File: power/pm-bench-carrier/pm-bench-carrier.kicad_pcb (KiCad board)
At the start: 2 copper layers, 130 x 55 mm, 45 parts, among them J1 VIN 40-60V, J2 VOUT 19V, Q1 2N7002, X1 PM-19V-200W, X2 Aux socket

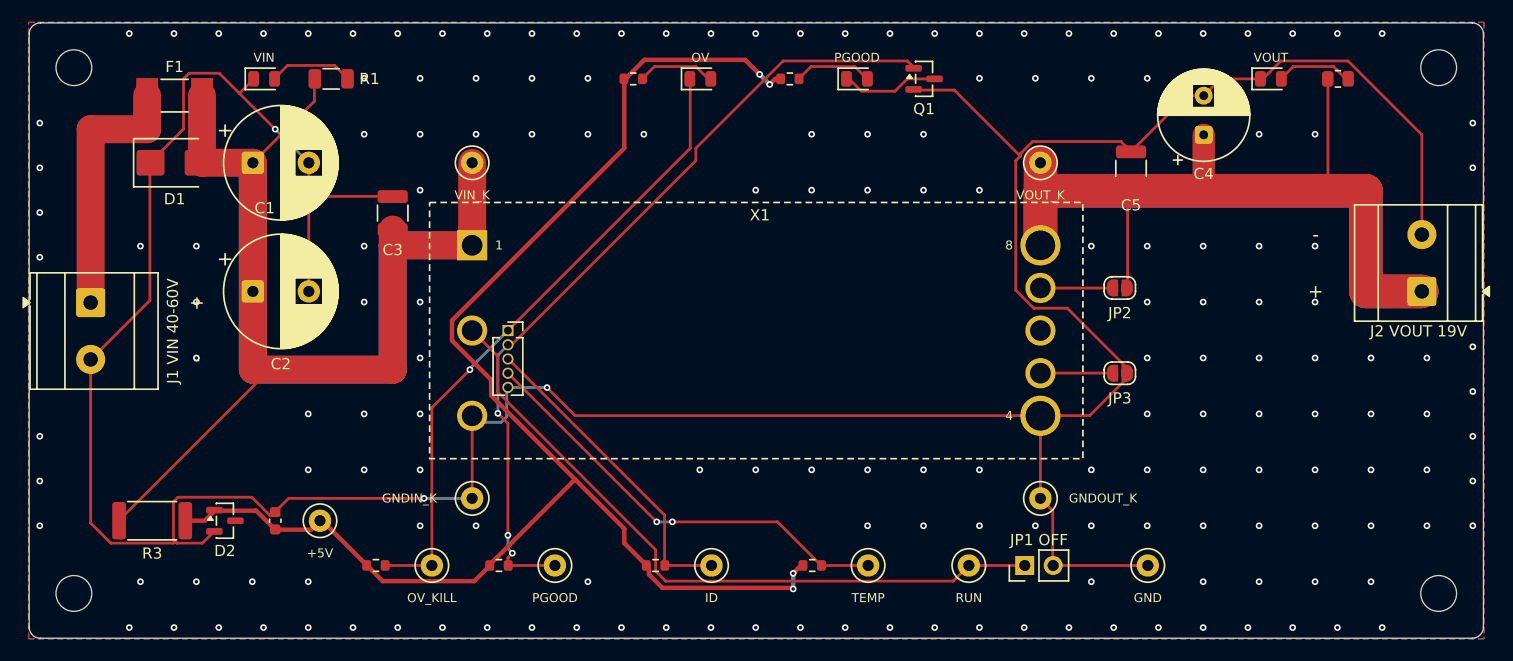
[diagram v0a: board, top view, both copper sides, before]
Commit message: pm-bench-carrier: pour GND before routing so KRT draws no GND tracks (zones kept via group power); DRC clean, 0 GND tracks
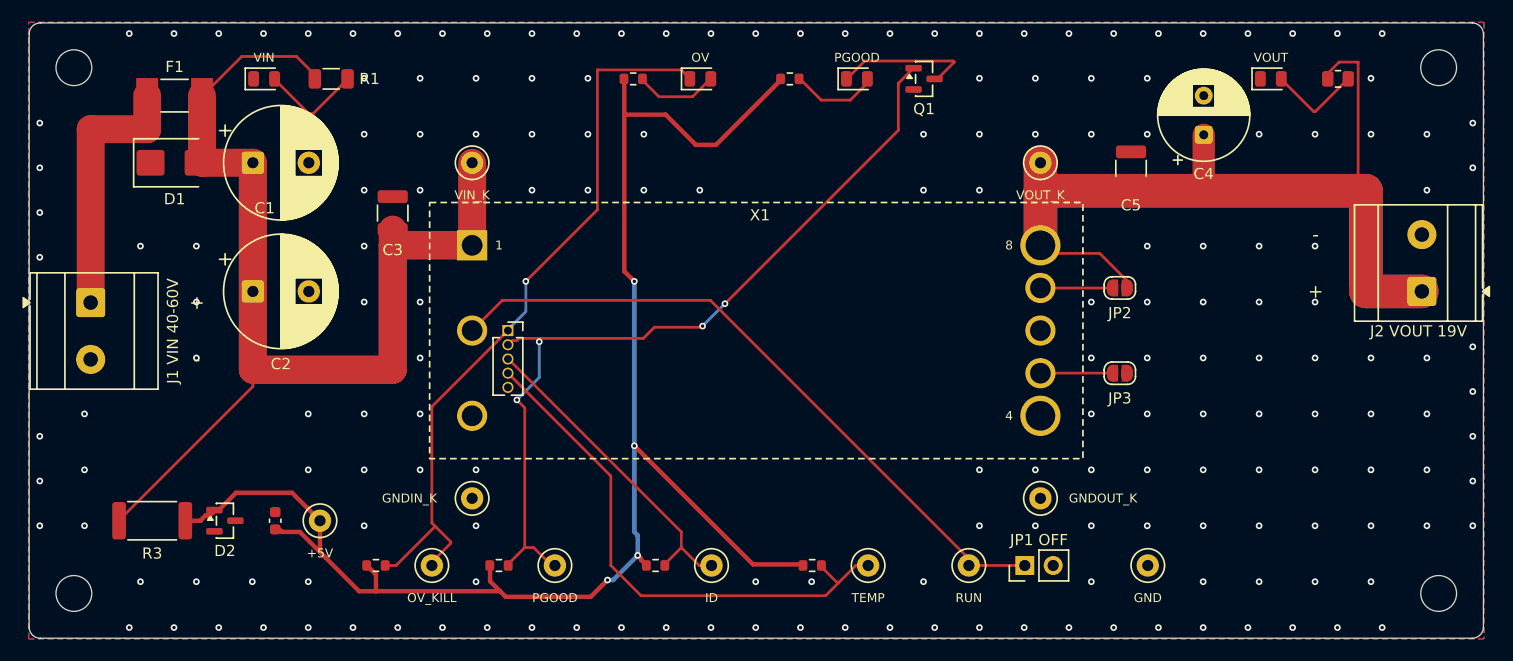
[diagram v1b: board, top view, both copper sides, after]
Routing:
- net GND: track 304.1 -> 0.00 mm, vias 172 -> 180
- net /TEMP: track 39.3 -> 48.4 mm, vias 2 -> 0
- net /OV_KILL: track 57.2 -> 66.0 mm
- net +5V: track 131.1 -> 139.1 mm
- net /VOUT: track 122.2 -> 128.4 mm
- net Net-(LED4-K): track 8.55 -> 12.4 mm
- net /RUN: track 62.2 -> 59.8 mm
- net /VIN: track 146.7 -> 148.4 mm
- net Net-(LED2-A): track 6.71 -> 8.40 mm
- net Net-(LED1-A): track 7.59 -> 9.17 mm
- net /PGOOD: track 72.4 -> 73.6 mm, vias 3 -> 4
- net Net-(LED3-A): track 6.81 -> 7.38 mm

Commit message: pm-bench-carrier: LCSC numbers on the SMD parts, fuse 10 A (0451010.MRL); jlcfab BOM/CPL filled
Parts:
- F1: value 8A 125V nano2 -> 10A 125V nano2
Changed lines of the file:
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@@
 			)
 		)
+		(property "LCSC" "C25803"
+			(at 0 0 0)
+			(layer "F.Fab")
+			(hide yes)
+			(effects
+				(font
+					(size 1.27 1.27)
+				)
+			)
+		)
 		(sheetname "pm-bench-carrier")
 		(sheetfile "pm-bench-carrier.kicad_sch")
@@
 			)
 		)
+		(property "LCSC" "C84256"
+			(at 0 0 0)
+			(layer "F.Fab")
+			(hide yes)
+			(effects
+				(font
+					(size 1.27 1.27)
+				)
+			)
+		)
 		(sheetname "pm-bench-carrier")
 		(sheetfile "pm-bench-carrier.kicad_sch")
@@
 			)
 		)
+		(property "LCSC" "C270956"
+			(at 0 0 0)
+			(layer "F.Fab")
+			(hide yes)
+			(effects
+				(font
+					(size 1.27 1.27)
+				)
+			)
+		)
 		(sheetname "pm-bench-carrier")
 		(sheetfile "pm-bench-carrier.kicad_sch")
@@
 			)
 		)
-		(property "Value" "8A 125V nano2"
+		(property "Value" "10A 125V nano2"
 			(at 0 2.7 0)
 			(unlocked yes)
@@
 			)
 		)
+		(property "LCSC" "C44479"
+			(at 0 0 0)
+			(layer "F.Fab")
+			(hide yes)
+			(effects
+				(font
+					(size 1.27 1.27)
+				)
+			)
+		)
 		(sheetname "pm-bench-carrier")
 		(sheetfile "pm-bench-carrier.kicad_sch")
@@
 			)
 		)
+		(property "LCSC" "C22978"
+			(at 0 0 0)
+			(layer "F.Fab")
+			(hide yes)
+			(effects
+				(font
+					(size 1.27 1.27)
+				)
+			)
+		)
 		(sheetname "pm-bench-carrier")
 		(sheetfile "pm-bench-carrier.kicad_sch")
@@
 			)
 		)
+		(property "LCSC" "C55151"
+			(at 0 0 0)
+			(layer "F.Fab")
+			(hide yes)
+			(effects
+				(font
+					(size 1.27 1.27)
+				)
+			)
+		)
 		(sheetname "pm-bench-carrier")
 		(sheetfile "pm-bench-carrier.kicad_sch")
@@
 			)
 		)
+		(property "LCSC" "C15849"
+			(at 0 0 0)
+			(layer "F.Fab")
+			(hide yes)
+			(effects
+				(font
+					(size 1.27 1.27)
+				)
+			)
+		)
 		(sheetname "pm-bench-carrier")
 		(sheetfile "pm-bench-carrier.kicad_sch")
@@
 			)
 		)
+		(property "LCSC" "C17943"
+			(at 0 0 0)
+			(layer "F.Fab")
+			(hide yes)
+			(effects
+				(font
+					(size 1.27 1.27)
+				)
+			)
+		)
 		(sheetname "pm-bench-carrier")
 		(sheetfile "pm-bench-carrier.kicad_sch")
@@
 			)
 		)
+		(property "LCSC" "C353345"
+			(at 0 0 0)
+			(layer "F.Fab")
+			(hide yes)
+			(effects
+				(font
+					(size 1.27 1.27)
+				)
+			)
+		)
 		(sheetname "pm-bench-carrier")
 		(sheetfile "pm-bench-carrier.kicad_sch")
@@
 			)
 		)
+		(property "LCSC" "C17414"
+			(at 0 0 0)
+			(layer "F.Fab")
+			(hide yes)
+			(effects
+				(font
+					(size 1.27 1.27)
+				)
+			)
+		)
 		(sheetname "pm-bench-carrier")
 		(sheetfile "pm-bench-carrier.kicad_sch")
@@
 			)
 		)
+		(property "LCSC" "C22978"
+			(at 0 0 0)
+			(layer "F.Fab")
+			(hide yes)
+			(effects
+				(font
+					(size 1.27 1.27)
+				)
+			)
+		)
 		(sheetname "pm-bench-carrier")
 		(sheetfile "pm-bench-carrier.kicad_sch")
@@
 			)
 		)
+		(property "LCSC" "C2297"
+			(at 0 0 0)
+			(layer "F.Fab")
+			(hide yes)
+			(effects
+				(font
+					(size 1.27 1.27)
+				)
+			)
+		)
 		(sheetname "pm-bench-carrier")
 		(sheetfile "pm-bench-carrier.kicad_sch")
@@
 			)
 		)
+		(property "LCSC" "C27131"
+			(at 0 0 0)
+			(layer "F.Fab")
+			(hide yes)
+			(effects
+				(font
+					(size 1.27 1.27)
+				)
+			)
+		)
 		(sheetname "pm-bench-carrier")
 		(sheetfile "pm-bench-carrier.kicad_sch")
@@
 			)
 		)
+		(property "LCSC" "C2297"
+			(at 0 0 0)
+			(layer "F.Fab")
+			(hide yes)
+			(effects
+				(font
+					(size 1.27 1.27)
+				)
+			)
+		)
 		(sheetname "pm-bench-carrier")
 		(sheetfile "pm-bench-carrier.kicad_sch")
@@
 			)
 		)
+		(property "LCSC" "C2297"
+			(at 0 0 0)
+			(layer "F.Fab")
+			(hide yes)
+			(effects
+				(font
+					(size 1.27 1.27)
+				)
+			)
+		)
 		(sheetname "pm-bench-carrier")
 		(sheetfile "pm-bench-carrier.kicad_sch")
@@
 			)
 		)
+		(property "LCSC" "C25804"
+			(at 0 0 0)
+			(layer "F.Fab")
+			(hide yes)
+			(effects
+				(font
+					(size 1.27 1.27)
+				)
+			)
+		)
 		(sheetname "pm-bench-carrier")
 		(sheetfile "pm-bench-carrier.kicad_sch")
@@
 			)
 		)
+		(property "LCSC" "C25803"
+			(at 0 0 0)
+			(layer "F.Fab")
+			(hide yes)
+			(effects
+				(font
+					(size 1.27 1.27)
+				)
+			)
+		)
 		(sheetname "pm-bench-carrier")
 		(sheetfile "pm-bench-carrier.kicad_sch")
@@
 			)
 		)
+		(property "LCSC" "C2918502"
+			(at 0 0 0)
+			(layer "F.Fab")
+			(hide yes)
+			(effects
+				(font
+					(size 1.27 1.27)
+				)
+			)
+		)
 		(sheetname "pm-bench-carrier")
 		(sheetfile "pm-bench-carrier.kicad_sch")
@@
 			)
 		)
+		(property "LCSC" "C8545"
+			(at 0 0 0)
+			(layer "F.Fab")
+			(hide yes)
+			(effects
+				(font
+					(size 1.27 1.27)
+				)
+			)
+		)
 		(sheetname "pm-bench-carrier")
 		(sheetfile "pm-bench-carrier.kicad_sch")
@@
 				)
 			)
+		)
+		(property "LCSC" "C25804"
+			(at 0 0 0)
+			(layer "F.Fab")
+			(hide yes)
+			(effects
+				(font
+					(size 1.27 1.27)
+				)
+			)

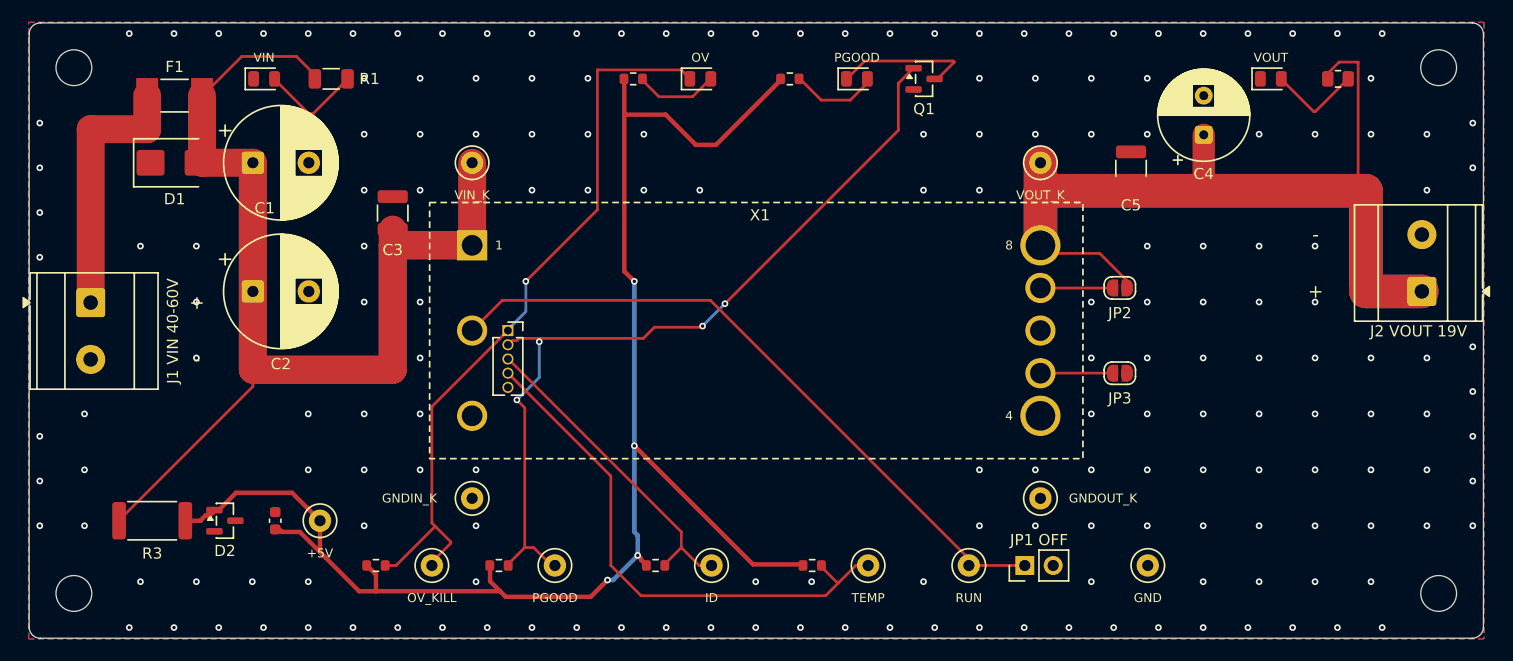
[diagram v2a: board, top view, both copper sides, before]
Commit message: pm-bench-carrier rev 0.2 board: screwed PM mount placed from pmmount.host_parts (SO1-SO4, PG1-PG6, MOD1 outline), trunks end on the standoffs, VOUT 4 mm for 13.2 A, Kelvin TPs at the screw x; rebuilt from the netlist and KRT-routed: DRC 0 errors, 0 unconnected, parity clean; docs and handoff updated
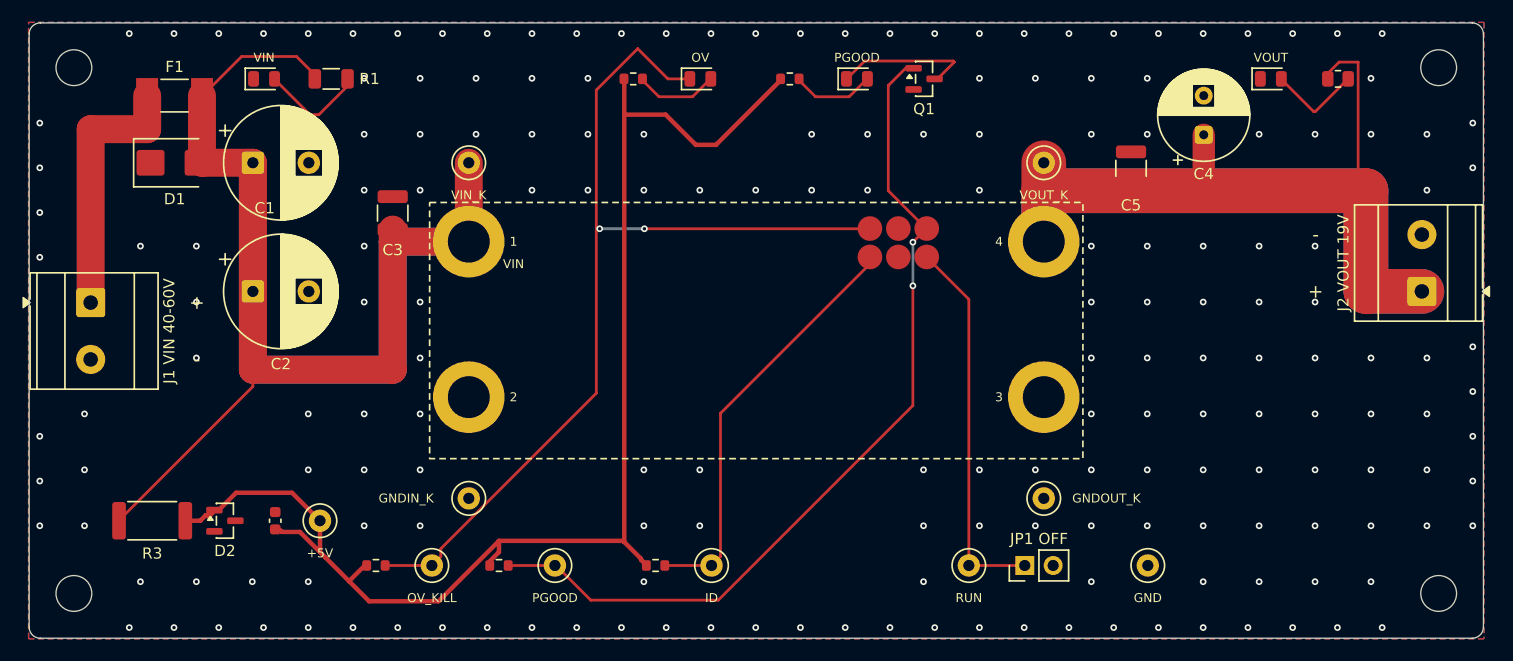
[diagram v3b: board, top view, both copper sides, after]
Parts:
- removed JP2: SENSE+, Jumper:SolderJumper-2_P1.3mm_Open_RoundedPad1.0x1.5mm
- removed JP3: SENSE-, Jumper:SolderJumper-2_P1.3mm_Open_RoundedPad1.0x1.5mm
- removed R9: 10k, Resistor_SMD:R_0603_1608Metric
- removed TP10: TEMP, TestPoint:TestPoint_Loop_D2.50mm_Drill1.0mm
- removed X1: PM-19V-200W, carrier:Brick_Eighth_DOSA_Socket
- removed X2: Aux socket, Connector_PinSocket_1.27mm:PinSocket_1x05_P1.27mm_Vertical
- added MOD1: PM_Module_Outline, carrier:PM_Module_Outline, F.Cu at (165.0, 127.5)
- added PG1: A1 OV_KILL, carrier:PM_Pogo_YZ130115073P, F.Cu at (175.2, 118.4)
- added PG2: A2 PGOOD, carrier:PM_Pogo_YZ130115073P, F.Cu at (180.2, 118.4)
- added PG3: A3 ID, carrier:PM_Pogo_YZ130115073P, F.Cu at (175.2, 120.9)
- added PG4: A4 RUN, carrier:PM_Pogo_YZ130115073P, F.Cu at (180.2, 120.9)
- added PG5: A5 GND, carrier:PM_Pogo_YZ130115073P, F.Cu at (177.7, 118.4)
- added PG6: A6 GND, carrier:PM_Pogo_YZ130115073P, F.Cu at (177.7, 120.9)
- added SO1: S1 VIN, carrier:PM_Standoff_M2x6_SMTSO, F.Cu at (139.3, 119.5)
- added SO2: S2 GND, carrier:PM_Standoff_M2x6_SMTSO, F.Cu at (139.3, 133.4)
- added SO3: S3 GND, carrier:PM_Standoff_M2x6_SMTSO, F.Cu at (190.7, 133.4)
- added SO4: S4 VOUT, carrier:PM_Standoff_M2x6_SMTSO, F.Cu at (190.7, 119.5)
- moved TP1 0.30 mm to (139.3, 112.5)
- moved TP2 0.30 mm to (139.3, 142.5)
- moved TP3 0.30 mm to (190.7, 112.5)
- moved TP4 0.30 mm to (190.7, 142.5)
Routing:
- net /TEMP: track 48.4 -> 0.00 mm
- net /RUN: track 59.8 -> 33.6 mm
- net /OV_KILL: track 66.0 -> 87.7 mm, vias 1 -> 2
- net +5V: track 139.1 -> 118.1 mm, vias 4 -> 0
- net /VOUT: track 128.4 -> 116.8 mm
- net /ID: track 28.8 -> 36.8 mm
- net Net-(JP3-A): track 6.00 -> 0.00 mm
- net Net-(JP2-A): track 6.00 -> 0.00 mm
- net /PGOOD: track 73.6 -> 77.0 mm, vias 4 -> 2
- net /VIN: track 148.4 -> 147.8 mm
- net GND: vias 180 -> 187
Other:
- board text removed: "TEMP"

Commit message: PM aux contacts: 2x3 1.27 mm SMT header (module J2, C41376035) into SMT socket (carrier J3, C41397112) replaces flat pads + pogos; standoffs M2 x 7 (C2916355), gap 7.0 mm. pmmount.py generates the new footprints; module J2 swapped in place, tools/route_aux.py moves PGOOD's via and adds a GND via between the columns (DRC as before, 0 unconnected, parity clean); carrier PG1-PG6 -> J3 and rebuilt by its flow (DRC 0 errors, 0 unconnected, parity clean); spec, ADR 0003 (6, 7), power-board.md and handoff updated; ID open = slot fault rule
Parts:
- removed PG1: A1 OV_KILL, carrier:PM_Pogo_YZ130115073P
- removed PG2: A2 PGOOD, carrier:PM_Pogo_YZ130115073P
- removed PG3: A3 ID, carrier:PM_Pogo_YZ130115073P
- removed PG4: A4 RUN, carrier:PM_Pogo_YZ130115073P
- removed PG5: A5 GND, carrier:PM_Pogo_YZ130115073P
- removed PG6: A6 GND, carrier:PM_Pogo_YZ130115073P
- added J3: Aux socket 2x3 1.27, carrier:PM_Aux_Socket_2x03_P1.27, F.Cu at (177.7, 119.7)
- SO1, SO2, SO3, SO4: footprint carrier:PM_Standoff_M2x6_SMTSO -> carrier:PM_Standoff_M2x7_SMTSO
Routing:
- net GND: track 0.00 -> 112.1 mm, vias 187 -> 171
- net Net-(LED3-A): track 7.38 -> 10.4 mm
- net /OV_KILL: track 87.7 -> 86.0 mm
- net /PGOOD: track 77.0 -> 75.9 mm, vias 2 -> 0
- net /ID: track 36.8 -> 37.8 mm
- net /VOUT: track 116.8 -> 117.3 mm

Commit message: 3D models: module aux header J2 on pm-19v-250w (hanxia HX PZ1.27-2x3P TP, C41376035; on B, offset sign follows the flip); unit U5 (stock VQFN-32 footprint points at a STEP KiCad does not ship: pp48 copy with the stock QFN-32 5x5 EP3.3 body), J201 XT60 (C98732), photoMOS U6 / U7 / U56 / U57 TLP176AM (C5370540) and opto U8 / U58 TLP291 (C55144, turned to its pin-1 dot) as pp48 footprint copies (stock models missing), FPIDs moved in uinput.py / unit.py and the board; carrier F1 nano2 fuse (C44479) as a carrier footprint copy; placement = pad fit of the LCSC footprint + the STEP-to-WRL origin shift (EasyEDA STEPs are not on the footprint origin, checked against the XT30 of 020591f), which also corrects today's aux socket (+0.3 mm z) and Degson terminal (-0.1 y, +0.2 z); renders checked; ERC 0 and DRC counts unchanged on unit, carrier, module
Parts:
- F1: footprint Fuse:Fuse_Littelfuse-NANO2-451_453 -> carrier:Fuse_Littelfuse-NANO2-451_453
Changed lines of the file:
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@@
 		(model "${KIPRJMOD}/carrier.3dshapes/PM_Aux_Socket_2x03_P1.27.step"
 			(offset
-				(xyz 0 0 0)
+				(xyz 0 0 0.3)
 			)
 			(scale
@@
 		)
 	)
-	(footprint "Fuse:Fuse_Littelfuse-NANO2-451_453"
+	(footprint "carrier:Fuse_Littelfuse-NANO2-451_453"
 		(layer "F.Cu")
 		(at 113 106.5)
@@
 		)
 		(embedded_fonts no)
-		(model "${KICAD10_3DMODEL_DIR}/Fuse.3dshapes/Fuse_Littelfuse-NANO2-451_453.step"
+		(model "${KIPRJMOD}/carrier.3dshapes/Fuse_Littelfuse-NANO2-451_453.step"
 			(offset
-				(xyz 0 0 0)
+				(xyz 0 0 1.35)
 			)
 			(scale
